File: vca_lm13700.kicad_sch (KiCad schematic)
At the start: 41 parts, among them Q201 Q_PNP_BEC, Q202 Q_PNP_BEC, U201 LM13700, U202 MCP6002, U203 TL072

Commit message: CV VCA & Mixer, Audio VCA schem capture
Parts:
- added C209: 100n, Capacitor_SMD:C_0603_1608Metric_Pad1.08x0.95mm_HandSolder, symbol Device:C
- U202, U203: footprint (none) -> Package_SO:SOIC-8_3.9x4.9mm_P1.27mm
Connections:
- net +9V: now also C209.1
- net GND: now also C209.2
- net VCA1_Iabc: now also U201.1; no longer U201.16
- net VCA2_Iabc: now also U201.16; no longer U201.1
- net at R210.2, RV203.1: now also U201.14 (+); no longer U201.3 (+)
- net at RV203.3: now also U201.13 (-); no longer U201.4 (-)
- net at R201.2, RV202.1: now also U201.3 (+); no longer U201.14 (+)
- net at RV202.3: now also U201.4 (-); no longer U201.13 (-)
- net at C203.1, R208.1: now also U201.8; no longer U201.9
- net at R202.2: now also U201.2 (DIODE_BIAS); no longer U201.15 (DIODE_BIAS)
- net at R211.2: now also U201.15 (DIODE_BIAS); no longer U201.2 (DIODE_BIAS)
- net at C208.1, R223.1: now also U201.9; no longer U201.8
- new net: R206.1, U201.5, U201.7
- new net: R222.1, U201.10, U201.12
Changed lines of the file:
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@@
   (junction (at 48.26 104.775) (diameter 0) (color 0 0 0 0)
   )
+  (junction (at 233.045 128.27) (diameter 0) (color 0 0 0 0)
+  )
+  (junction (at 233.045 143.51) (diameter 0) (color 0 0 0 0)
+  )
   (junction (at 243.84 143.51) (diameter 0) (color 0 0 0 0)
   )
@@
     (stroke (width 0) (type default) (color 0 0 0 0))
   )
+  (wire (pts (xy 222.25 139.7) (xy 222.25 143.51))
+    (stroke (width 0) (type default) (color 0 0 0 0))
+  )
   (wire (pts (xy 118.11 50.8) (xy 123.825 50.8))
     (stroke (width 0) (type default) (color 0 0 0 0))
@@
     (stroke (width 0) (type default) (color 0 0 0 0))
   )
+  (wire (pts (xy 222.25 128.27) (xy 233.045 128.27))
+    (stroke (width 0) (type default) (color 0 0 0 0))
+  )
   (wire (pts (xy 233.045 128.27) (xy 233.045 132.08))
     (stroke (width 0) (type default) (color 0 0 0 0))
@@
     (stroke (width 0) (type default) (color 0 0 0 0))
   )
+  (wire (pts (xy 222.25 132.08) (xy 222.25 128.27))
+    (stroke (width 0) (type default) (color 0 0 0 0))
+  )
   (wire (pts (xy 73.66 104.775) (xy 73.66 114.935))
     (stroke (width 0) (type default) (color 0 0 0 0))
@@
   )
   (wire (pts (xy 170.18 132.715) (xy 173.99 132.715))
+    (stroke (width 0) (type default) (color 0 0 0 0))
+  )
+  (wire (pts (xy 222.25 143.51) (xy 233.045 143.51))
     (stroke (width 0) (type default) (color 0 0 0 0))
   )
@@
     (property "Reference" "U202" (id 0) (at 181.61 119.38 0))
     (property "Value" "MCP6002" (id 1) (at 181.61 121.92 0))
-    (property "Footprint" "" (id 2) (at 181.61 130.175 0)
+    (property "Footprint" "Package_SO:SOIC-8_3.9x4.9mm_P1.27mm" (id 2) (at 181.61 130.175 0)
       (effects (font (size 1.27 1.27)) hide)
     )
@@
       (effects (font (size 1.27 1.27)) (justify left))
     )
-    (property "Footprint" "" (id 2) (at 257.175 135.89 0)
+    (property "Footprint" "Package_SO:SOIC-8_3.9x4.9mm_P1.27mm" (id 2) (at 257.175 135.89 0)
       (effects (font (size 1.27 1.27)) hide)
     )
@@
     (pin "3")
   )
-  (symbol (lib_id "Amplifier_Operational:LM13700") (at 115.57 48.26 0) (unit 2)
+  (symbol (lib_id "Amplifier_Operational:LM13700") (at 115.57 48.26 0) (unit 4)
     (in_bom yes) (on_board yes) (fields_autoplaced)
     (property "Reference" "U201" (id 0) (at 113.03 38.1 0))
@@
       (effects (font (size 1.27 1.27)) (justify left))
     )
-    (property "Footprint" "" (id 2) (at 276.86 135.89 0)
+    (property "Footprint" "Package_SO:SOIC-8_3.9x4.9mm_P1.27mm" (id 2) (at 276.86 135.89 0)
       (effects (font (size 1.27 1.27)) hide)
     )
@@
     (property "Reference" "U202" (id 0) (at 55.88 119.38 0))
     (property "Value" "MCP6002" (id 1) (at 55.88 121.92 0))
-    (property "Footprint" "" (id 2) (at 55.88 130.175 0)
+    (property "Footprint" "Package_SO:SOIC-8_3.9x4.9mm_P1.27mm" (id 2) (at 55.88 130.175 0)
       (effects (font (size 1.27 1.27)) hide)
     )
@@
     (pin "2")
   )
-  (symbol (lib_id "Amplifier_Operational:LM13700") (at 92.71 48.26 0) (unit 1)
+  (symbol (lib_id "Amplifier_Operational:LM13700") (at 92.71 48.26 0) (unit 3)
     (in_bom yes) (on_board yes) (fields_autoplaced)
     (property "Reference" "U201" (id 0) (at 92.71 38.1 0))
@@
     (pin "6")
   )
-  (symbol (lib_id "Amplifier_Operational:LM13700") (at 227.965 48.26 0) (unit 3)
+  (symbol (lib_id "Amplifier_Operational:LM13700") (at 227.965 48.26 0) (unit 1)
     (in_bom yes) (on_board yes) (fields_autoplaced)
     (property "Reference" "U201" (id 0) (at 227.965 38.1 0))
@@
     (property "Reference" "U203" (id 0) (at 187.325 53.34 0))
     (property "Value" "TL072" (id 1) (at 187.325 55.88 0))
-    (property "Footprint" "" (id 2) (at 187.325 63.5 0)
+    (property "Footprint" "Package_SO:SOIC-8_3.9x4.9mm_P1.27mm" (id 2) (at 187.325 63.5 0)
       (effects (font (size 1.27 1.27)) hide)
     )
@@
     (pin "2")
   )
-  (symbol (lib_id "Amplifier_Operational:LM13700") (at 257.175 48.26 0) (unit 4)
+  (symbol (lib_id "Amplifier_Operational:LM13700") (at 257.175 48.26 0) (unit 2)
     (in_bom yes) (on_board yes) (fields_autoplaced)
     (property "Reference" "U201" (id 0) (at 254.635 38.1 0))
@@
     (pin "2")
   )
+  (symbol (lib_id "Device:C") (at 222.25 135.89 0) (unit 1)
+    (in_bom yes) (on_board yes) (fields_autoplaced)
+    (property "Reference" "C209" (id 0) (at 226.06 134.6199 0)
+      (effects (font (size 1.27 1.27)) (justify left))
+    )
+    (property "Value" "100n" (id 1) (at 226.06 137.1599 0)
+      (effects (font (size 1.27 1.27)) (justify left))
+    )
+    (property "Footprint" "Capacitor_SMD:C_0603_1608Metric_Pad1.08x0.95mm_HandSolder" (id 2) (at 223.2152 139.7 0)
+      (effects (font (size 1.27 1.27)) hide)
+    )
+    (property "Datasheet" "~" (id 3) (at 222.25 135.89 0)
+      (effects (font (size 1.27 1.27)) hide)
+    )
+    (pin "1")
+    (pin "2")
+  )
   (symbol (lib_id "Device:R") (at 161.29 69.85 0) (unit 1)
     (in_bom yes) (on_board yes)
@@
     (property "Reference" "U203" (id 0) (at 52.07 53.34 0))
     (property "Value" "TL072" (id 1) (at 52.07 55.88 0))
-    (property "Footprint" "" (id 2) (at 52.07 63.5 0)
-      (effects (font (size 1.27 1.27)) hide)
-    )
+    (property "Footprint" "Package_SO:SOIC-8_3.9x4.9mm_P1.27mm" (id 2) (at 52.07 63.5 0)
+      (effects (font (size 1.27 1.27)) hide)
+    )

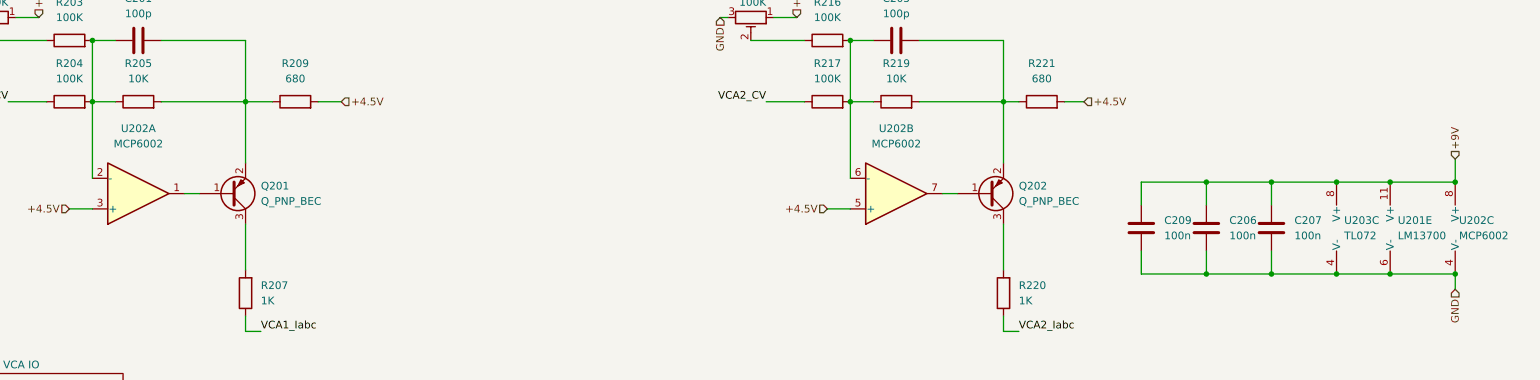
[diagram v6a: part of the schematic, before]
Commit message: LFO schem capture done / replace r2r opamps
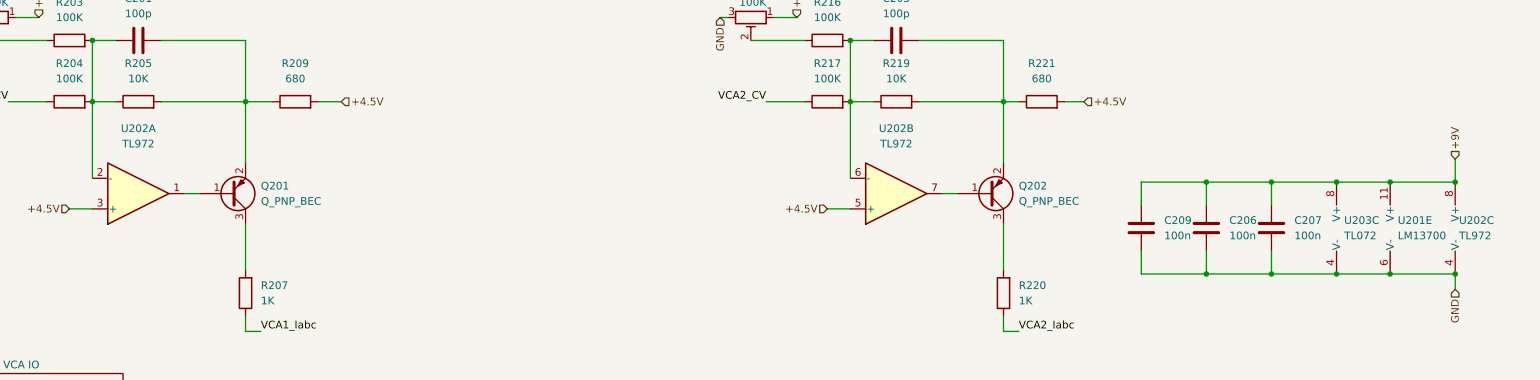
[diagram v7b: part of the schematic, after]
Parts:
- U202: value MCP6002 -> TL972
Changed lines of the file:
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@@
     (in_bom yes) (on_board yes) (fields_autoplaced)
     (property "Reference" "U202" (id 0) (at 181.61 119.38 0))
-    (property "Value" "MCP6002" (id 1) (at 181.61 121.92 0))
+    (property "Value" "TL972" (id 1) (at 181.61 121.92 0))
     (property "Footprint" "Package_SO:SOIC-8_3.9x4.9mm_P1.27mm" (id 2) (at 181.61 130.175 0)
       (effects (font (size 1.27 1.27)) hide)
@@
       (effects (font (size 1.27 1.27)) (justify left))
     )
-    (property "Value" "MCP6002" (id 1) (at 274.955 137.1599 0)
+    (property "Value" "TL972" (id 1) (at 274.955 137.1599 0)
       (effects (font (size 1.27 1.27)) (justify left))
     )
@@
     (in_bom yes) (on_board yes) (fields_autoplaced)
     (property "Reference" "U202" (id 0) (at 55.88 119.38 0))
-    (property "Value" "MCP6002" (id 1) (at 55.88 121.92 0))
+    (property "Value" "TL972" (id 1) (at 55.88 121.92 0))
     (property "Footprint" "Package_SO:SOIC-8_3.9x4.9mm_P1.27mm" (id 2) (at 55.88 130.175 0)
       (effects (font (size 1.27 1.27)) hide)

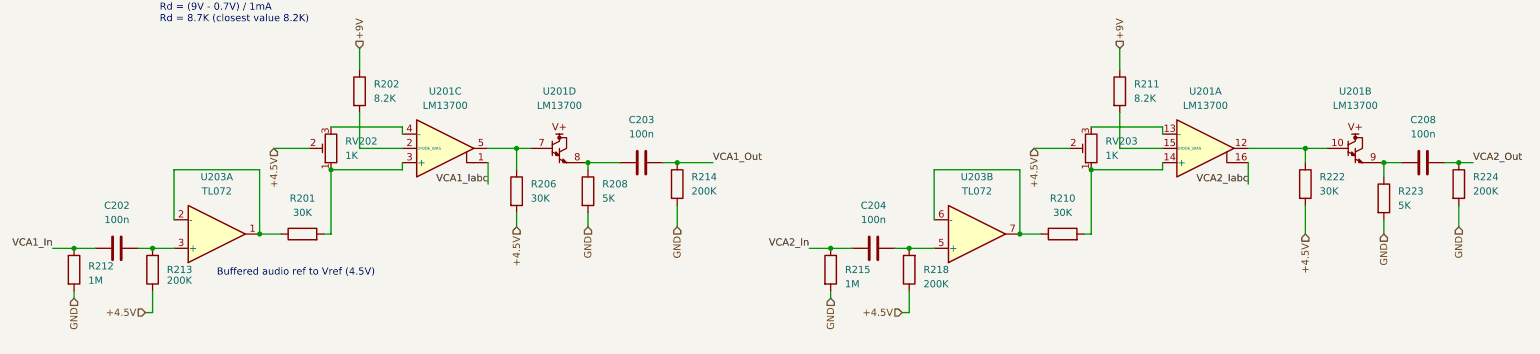
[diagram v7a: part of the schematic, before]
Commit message: Increase the size of dc blocking caps
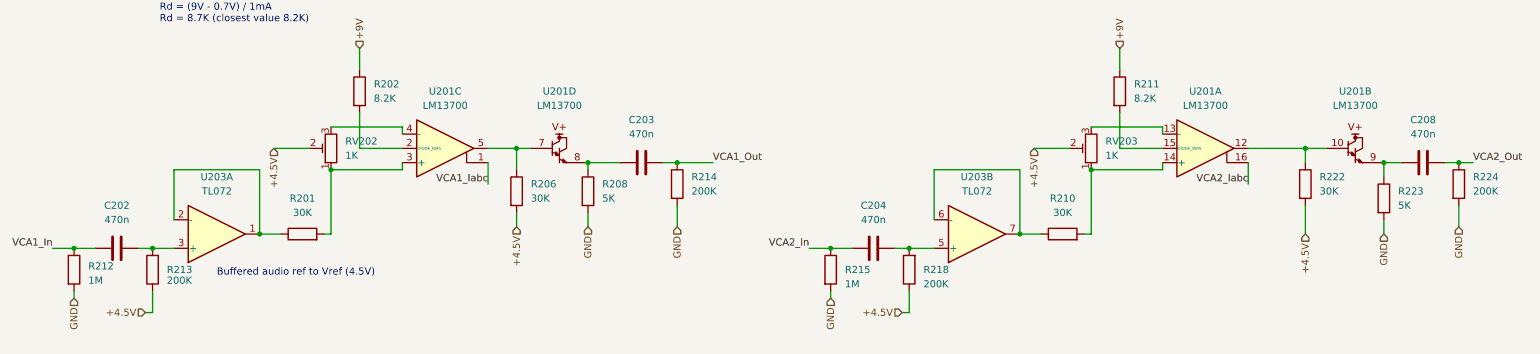
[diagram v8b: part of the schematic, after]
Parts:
- C202, C203, C204, C208: value 100n -> 470n; footprint Capacitor_SMD:C_0603_1608Metric_Pad1.08x0.95mm_HandSolder -> Capacitor_SMD:C_0805_2012Metric_Pad1.18x1.45mm_HandSolder
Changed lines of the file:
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@@
-    (pin "2")
-  )
-  (symbol (lib_id "Device:C") (at 168.91 66.04 90) (unit 1)
-    (in_bom yes) (on_board yes) (fields_autoplaced)
-    (property "Reference" "C204" (id 0) (at 168.91 58.42 90))
-    (property "Value" "100n" (id 1) (at 168.91 60.96 90))
-    (property "Footprint" "Capacitor_SMD:C_0603_1608Metric_Pad1.08x0.95mm_HandSolder" (id 2) (at 172.72 65.0748 0)
-      (effects (font (size 1.27 1.27)) hide)
-    )
-    (property "Datasheet" "~" (id 3) (at 168.91 66.04 0)
-      (effects (font (size 1.27 1.27)) hide)
-    )
-    (pin "1")
     (pin "2")
   )
@@
     (pin "4")
     (pin "8")
+  )
+  (symbol (lib_id "Device:C") (at 34.29 66.04 90) (unit 1)
+    (in_bom yes) (on_board yes) (fields_autoplaced)
+    (property "Reference" "C202" (id 0) (at 34.29 58.42 90))
+    (property "Value" "470n" (id 1) (at 34.29 60.96 90))
+    (property "Footprint" "Capacitor_SMD:C_0805_2012Metric_Pad1.18x1.45mm_HandSolder" (id 2) (at 38.1 65.0748 0)
+      (effects (font (size 1.27 1.27)) hide)
+    )
+    (property "Datasheet" "~" (id 3) (at 34.29 66.04 0)
+      (effects (font (size 1.27 1.27)) hide)
+    )
+    (pin "1")
+    (pin "2")
   )
   (symbol (lib_id "Device:R") (at 202.565 63.5 90) (unit 1)
@@
     (pin "3")
   )
+  (symbol (lib_id "Device:C") (at 168.91 66.04 90) (unit 1)
+    (in_bom yes) (on_board yes) (fields_autoplaced)
+    (property "Reference" "C204" (id 0) (at 168.91 58.42 90))
+    (property "Value" "470n" (id 1) (at 168.91 60.96 90))
+    (property "Footprint" "Capacitor_SMD:C_0805_2012Metric_Pad1.18x1.45mm_HandSolder" (id 2) (at 172.72 65.0748 0)
+      (effects (font (size 1.27 1.27)) hide)
+    )
+    (property "Datasheet" "~" (id 3) (at 168.91 66.04 0)
+      (effects (font (size 1.27 1.27)) hide)
+    )
+    (pin "1")
+    (pin "2")
+  )
   (symbol (lib_id "Amplifier_Operational:LM13700") (at 115.57 48.26 0) (unit 4)
     (in_bom yes) (on_board yes) (fields_autoplaced)
@@
     (pin "6")
   )
-  (symbol (lib_id "Device:C") (at 34.29 66.04 90) (unit 1)
-    (in_bom yes) (on_board yes) (fields_autoplaced)
-    (property "Reference" "C202" (id 0) (at 34.29 58.42 90))
-    (property "Value" "100n" (id 1) (at 34.29 60.96 90))
-    (property "Footprint" "Capacitor_SMD:C_0603_1608Metric_Pad1.08x0.95mm_HandSolder" (id 2) (at 38.1 65.0748 0)
-      (effects (font (size 1.27 1.27)) hide)
-    )
-    (property "Datasheet" "~" (id 3) (at 34.29 66.04 0)
-      (effects (font (size 1.27 1.27)) hide)
-    )
-    (pin "1")
-    (pin "2")
-  )
   (symbol (lib_id "Device:R") (at 273.05 54.61 0) (unit 1)
     (in_bom yes) (on_board yes) (fields_autoplaced)
@@
     (pin "2")
   )
+  (symbol (lib_id "Device:C") (at 266.7 50.8 90) (unit 1)
+    (in_bom yes) (on_board yes) (fields_autoplaced)
+    (property "Reference" "C208" (id 0) (at 266.7 43.18 90))
+    (property "Value" "470n" (id 1) (at 266.7 45.72 90))
+    (property "Footprint" "Capacitor_SMD:C_0805_2012Metric_Pad1.18x1.45mm_HandSolder" (id 2) (at 270.51 49.8348 0)
+      (effects (font (size 1.27 1.27)) hide)
+    )
+    (property "Datasheet" "~" (id 3) (at 266.7 50.8 0)
+      (effects (font (size 1.27 1.27)) hide)
+    )
+    (pin "1")
+    (pin "2")
+  )
   (symbol (lib_id "Amplifier_Operational:LM13700") (at 257.175 48.26 0) (unit 2)
     (in_bom yes) (on_board yes) (fields_autoplaced)
@@
     (in_bom yes) (on_board yes) (fields_autoplaced)
     (property "Reference" "C203" (id 0) (at 127.635 43.18 90))
-    (property "Value" "100n" (id 1) (at 127.635 45.72 90))
-    (property "Footprint" "Capacitor_SMD:C_0603_1608Metric_Pad1.08x0.95mm_HandSolder" (id 2) (at 131.445 49.8348 0)
+    (property "Value" "470n" (id 1) (at 127.635 45.72 90))
+    (property "Footprint" "Capacitor_SMD:C_0805_2012Metric_Pad1.18x1.45mm_HandSolder" (id 2) (at 131.445 49.8348 0)
       (effects (font (size 1.27 1.27)) hide)
     )
@@
     (pin "8")
   )
-  (symbol (lib_id "Device:C") (at 266.7 50.8 90) (unit 1)
-    (in_bom yes) (on_board yes) (fields_autoplaced)
-    (property "Reference" "C208" (id 0) (at 266.7 43.18 90))
-    (property "Value" "100n" (id 1) (at 266.7 45.72 90))
-    (property "Footprint" "Capacitor_SMD:C_0603_1608Metric_Pad1.08x0.95mm_HandSolder" (id 2) (at 270.51 49.8348 0)
-      (effects (font (size 1.27 1.27)) hide)
-    )
-    (property "Datasheet" "~" (id 3) (at 266.7 50.8 0)
-      (effects (font (size 1.27 1.27)) hide)
-    )
-    (pin "1")
-    (pin "2")
-  )
   (sheet (at 27.94 160.02) (size 25.4 21.59) (fields_autoplaced)
